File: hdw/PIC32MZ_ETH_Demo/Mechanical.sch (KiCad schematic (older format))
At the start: 24 parts

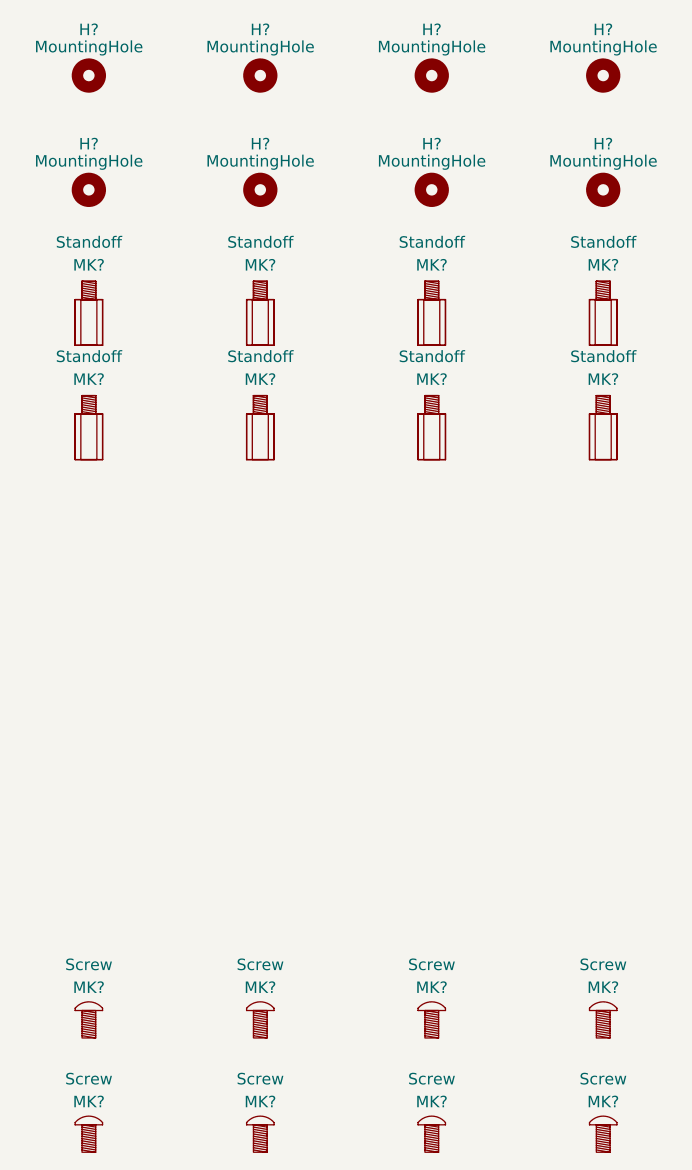
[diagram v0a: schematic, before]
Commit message: More schematic tweaks, followed PHY design guide
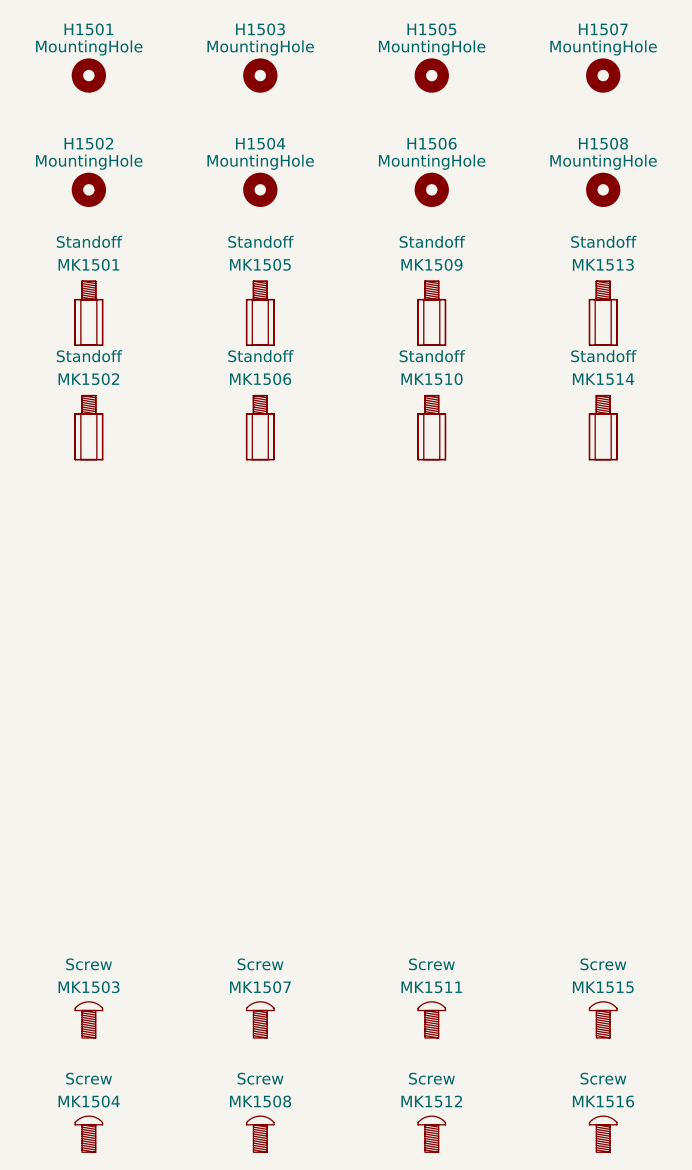
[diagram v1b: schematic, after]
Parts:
- gave numbers to parts that had none: 24
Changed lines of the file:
@@
 EESchema Schematic File Version 4
+LIBS:PIC32MZ_ETH_Demo-cache
 EELAYER 30 0
 EELAYER END
@@
 $EndDescr
 $Comp
-L Mechanical:MountingHole H?
+L Mechanical:MountingHole H1501
 U 1 1 5CC525BF
 P 4070 1580
-F 0 "H?" H 4070 1780 50  0000 C CNN
+F 0 "H1501" H 4070 1780 50  0000 C CNN
 F 1 "MountingHole" H 4070 1705 50  0000 C CNN
 F 2 "MountingHole:MountingHole_3mm" H 4070 1580 50  0001 C CNN
@@
 $EndComp
 $Comp
-L Mechanical:MountingHole H?
+L Mechanical:MountingHole H1503
 U 1 1 5CC5295F
 P 4820 1580
-F 0 "H?" H 4820 1780 50  0000 C CNN
+F 0 "H1503" H 4820 1780 50  0000 C CNN
 F 1 "MountingHole" H 4820 1705 50  0000 C CNN
 F 2 "MountingHole:MountingHole_3mm" H 4820 1580 50  0001 C CNN
@@
 $EndComp
 $Comp
-L Mechanical:MountingHole H?
+L Mechanical:MountingHole H1505
 U 1 1 5CC52BE4
 P 5570 1580
-F 0 "H?" H 5570 1780 50  0000 C CNN
+F 0 "H1505" H 5570 1780 50  0000 C CNN
 F 1 "MountingHole" H 5570 1705 50  0000 C CNN
 F 2 "MountingHole:MountingHole_3mm" H 5570 1580 50  0001 C CNN
@@
 $EndComp
 $Comp
-L Mechanical:MountingHole H?
+L Mechanical:MountingHole H1507
 U 1 1 5CC530EC
 P 6320 1580
-F 0 "H?" H 6320 1780 50  0000 C CNN
+F 0 "H1507" H 6320 1780 50  0000 C CNN
 F 1 "MountingHole" H 6320 1705 50  0000 C CNN
 F 2 "MountingHole:MountingHole_3mm" H 6320 1580 50  0001 C CNN
@@
 $EndComp
 $Comp
-L Mechanical:MountingHole H?
+L Mechanical:MountingHole H1502
 U 1 1 5CC53950
 P 4070 2080
-F 0 "H?" H 4070 2280 50  0000 C CNN
+F 0 "H1502" H 4070 2280 50  0000 C CNN
 F 1 "MountingHole" H 4070 2205 50  0000 C CNN
 F 2 "MountingHole:MountingHole_3mm" H 4070 2080 50  0001 C CNN
@@
 $EndComp
 $Comp
-L Mechanical:MountingHole H?
+L Mechanical:MountingHole H1504
 U 1 1 5CC5395A
 P 4820 2080
-F 0 "H?" H 4820 2280 50  0000 C CNN
+F 0 "H1504" H 4820 2280 50  0000 C CNN
 F 1 "MountingHole" H 4820 2205 50  0000 C CNN
 F 2 "MountingHole:MountingHole_3mm" H 4820 2080 50  0001 C CNN
@@
 $EndComp
 $Comp
-L Mechanical:MountingHole H?
+L Mechanical:MountingHole H1506
 U 1 1 5CC53964
 P 5570 2080
-F 0 "H?" H 5570 2280 50  0000 C CNN
+F 0 "H1506" H 5570 2280 50  0000 C CNN
 F 1 "MountingHole" H 5570 2205 50  0000 C CNN
 F 2 "MountingHole:MountingHole_3mm" H 5570 2080 50  0001 C CNN
@@
 $EndComp
 $Comp
-L Mechanical:MountingHole H?
+L Mechanical:MountingHole H1508
 U 1 1 5CC5396E
 P 6320 2080
-F 0 "H?" H 6320 2280 50  0000 C CNN
+F 0 "H1508" H 6320 2280 50  0000 C CNN
 F 1 "MountingHole" H 6320 2205 50  0000 C CNN
 F 2 "MountingHole:MountingHole_3mm" H 6320 2080 50  0001 C CNN
@@
 $EndComp
 $Comp
-L Custom_Library:Standoff MK?
+L Custom_Library:Standoff MK1501
 U 1 1 5CC56F37
 P 4070 2560
-F 0 "MK?" H 4070 2710 50  0000 C CNN
+F 0 "MK1501" H 4070 2710 50  0000 C CNN
 F 1 "Standoff" H 4070 2810 50  0000 C CNN
 F 2 "" H 4070 2910 50  0001 C CNN
@@
 $EndComp
 $Comp
-L Custom_Library:Standoff MK?
+L Custom_Library:Standoff MK1505
 U 1 1 5CC579C0
 P 4820 2560
-F 0 "MK?" H 4820 2710 50  0000 C CNN
+F 0 "MK1505" H 4820 2710 50  0000 C CNN
 F 1 "Standoff" H 4820 2810 50  0000 C CNN
 F 2 "" H 4820 2910 50  0001 C CNN
@@
 $EndComp
 $Comp
-L Custom_Library:Standoff MK?
+L Custom_Library:Standoff MK1509
 U 1 1 5CC58B78
 P 5570 2560
-F 0 "MK?" H 5570 2710 50  0000 C CNN
+F 0 "MK1509" H 5570 2710 50  0000 C CNN
 F 1 "Standoff" H 5570 2810 50  0000 C CNN
 F 2 "" H 5570 2910 50  0001 C CNN
@@
 $EndComp
 $Comp
-L Custom_Library:Standoff MK?
+L Custom_Library:Standoff MK1513
 U 1 1 5CC59CF0
 P 6320 2560
-F 0 "MK?" H 6320 2710 50  0000 C CNN
+F 0 "MK1513" H 6320 2710 50  0000 C CNN
 F 1 "Standoff" H 6320 2810 50  0000 C CNN
 F 2 "" H 6320 2910 50  0001 C CNN
@@
 $EndComp
 $Comp
-L Custom_Library:Standoff MK?
+L Custom_Library:Standoff MK1502
 U 1 1 5CC5B024
 P 4070 3060
-F 0 "MK?" H 4070 3210 50  0000 C CNN
+F 0 "MK1502" H 4070 3210 50  0000 C CNN
 F 1 "Standoff" H 4070 3310 50  0000 C CNN
 F 2 "" H 4070 3410 50  0001 C CNN
@@
 $EndComp
 $Comp
-L Custom_Library:Standoff MK?
+L Custom_Library:Standoff MK1506
 U 1 1 5CC5B02E
 P 4820 3060
-F 0 "MK?" H 4820 3210 50  0000 C CNN
+F 0 "MK1506" H 4820 3210 50  0000 C CNN
 F 1 "Standoff" H 4820 3310 50  0000 C CNN
 F 2 "" H 4820 3410 50  0001 C CNN
@@
 $EndComp
 $Comp
-L Custom_Library:Standoff MK?
+L Custom_Library:Standoff MK1510
 U 1 1 5CC5B038
 P 5570 3060
-F 0 "MK?" H 5570 3210 50  0000 C CNN
+F 0 "MK1510" H 5570 3210 50  0000 C CNN
 F 1 "Standoff" H 5570 3310 50  0000 C CNN
 F 2 "" H 5570 3410 50  0001 C CNN
@@
 $EndComp
 $Comp
-L Custom_Library:Standoff MK?
+L Custom_Library:Standoff MK1514
 U 1 1 5CC5B042
 P 6320 3060
-F 0 "MK?" H 6320 3210 50  0000 C CNN
+F 0 "MK1514" H 6320 3210 50  0000 C CNN
 F 1 "Standoff" H 6320 3310 50  0000 C CNN
 F 2 "" H 6320 3410 50  0001 C CNN
@@
 $EndComp
 $Comp
-L Custom_Library:Screw MK?
+L Custom_Library:Screw MK1503
 U 1 1 5CC6CBF3
 P 4070 5670
-F 0 "MK?" H 4070 5770 50  0000 C CNN
+F 0 "MK1503" H 4070 5770 50  0000 C CNN
 F 1 "Screw" H 4070 5870 50  0000 C CNN
 F 2 "" H 4070 5920 50  0001 C CNN
@@
 $EndComp
 $Comp
-L Custom_Library:Screw MK?
+L Custom_Library:Screw MK1507
 U 1 1 5CC6D1A5
 P 4820 5670
-F 0 "MK?" H 4820 5770 50  0000 C CNN
+F 0 "MK1507" H 4820 5770 50  0000 C CNN
 F 1 "Screw" H 4820 5870 50  0000 C CNN
 F 2 "" H 4820 5920 50  0001 C CNN
@@
 $EndComp
 $Comp
-L Custom_Library:Screw MK?
+L Custom_Library:Screw MK1511
 U 1 1 5CC6E4BD
 P 5570 5670
-F 0 "MK?" H 5570 5770 50  0000 C CNN
+F 0 "MK1511" H 5570 5770 50  0000 C CNN
 F 1 "Screw" H 5570 5870 50  0000 C CNN
 F 2 "" H 5570 5920 50  0001 C CNN
@@
 $EndComp
 $Comp
-L Custom_Library:Screw MK?
+L Custom_Library:Screw MK1515
 U 1 1 5CC6F609
 P 6320 5670
-F 0 "MK?" H 6320 5770 50  0000 C CNN
+F 0 "MK1515" H 6320 5770 50  0000 C CNN
 F 1 "Screw" H 6320 5870 50  0000 C CNN
 F 2 "" H 6320 5920 50  0001 C CNN
@@
 $EndComp
 $Comp
-L Custom_Library:Screw MK?
+L Custom_Library:Screw MK1504
 U 1 1 5CC70A99
 P 4070 6170
-F 0 "MK?" H 4070 6270 50  0000 C CNN
+F 0 "MK1504" H 4070 6270 50  0000 C CNN
 F 1 "Screw" H 4070 6370 50  0000 C CNN
 F 2 "" H 4070 6420 50  0001 C CNN
@@
 $EndComp
 $Comp
-L Custom_Library:Screw MK?
+L Custom_Library:Screw MK1508
 U 1 1 5CC70AA3
 P 4820 6170
-F 0 "MK?" H 4820 6270 50  0000 C CNN
+F 0 "MK1508" H 4820 6270 50  0000 C CNN
 F 1 "Screw" H 4820 6370 50  0000 C CNN
 F 2 "" H 4820 6420 50  0001 C CNN
@@
 $EndComp
 $Comp
-L Custom_Library:Screw MK?
+L Custom_Library:Screw MK1512
 U 1 1 5CC70AAD
 P 5570 6170
-F 0 "MK?" H 5570 6270 50  0000 C CNN
+F 0 "MK1512" H 5570 6270 50  0000 C CNN
 F 1 "Screw" H 5570 6370 50  0000 C CNN
 F 2 "" H 5570 6420 50  0001 C CNN
@@
 $EndComp
 $Comp
-L Custom_Library:Screw MK?
+L Custom_Library:Screw MK1516
 U 1 1 5CC70AB7
 P 6320 6170
-F 0 "MK?" H 6320 6270 50  0000 C CNN
+F 0 "MK1516" H 6320 6270 50  0000 C CNN
 F 1 "Screw" H 6320 6370 50  0000 C CNN
 F 2 "" H 6320 6420 50  0001 C CNN

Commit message: Finished board layout
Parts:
- removed H1506, H1507, H1508: MountingHole, MountingHole:MountingHole_3mm, symbol Mechanical:MountingHole
- removed MK1510, MK1513, MK1514: Standoff, symbol Custom_Library:Standoff
- removed MK1512, MK1515, MK1516: Screw, symbol Custom_Library:Screw
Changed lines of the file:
@@
-$EndComp
-$Comp
-L Mechanical:MountingHole H1507
-U 1 1 5CC530EC
-P 6320 1580
-F 0 "H1507" H 6320 1780 50  0000 C CNN
-F 1 "MountingHole" H 6320 1705 50  0000 C CNN
-F 2 "MountingHole:MountingHole_3mm" H 6320 1580 50  0001 C CNN
-F 3 "~" H 6320 1580 50  0001 C CNN
-	1    6320 1580
-	1    0    0    -1
 $EndComp
 $Comp
@@
 F 3 "~" H 4820 2080 50  0001 C CNN
 	1    4820 2080
-	1    0    0    -1
-$EndComp
-$Comp
-L Mechanical:MountingHole H1506
-U 1 1 5CC53964
-P 5570 2080
-F 0 "H1506" H 5570 2280 50  0000 C CNN
-F 1 "MountingHole" H 5570 2205 50  0000 C CNN
-F 2 "MountingHole:MountingHole_3mm" H 5570 2080 50  0001 C CNN
-F 3 "~" H 5570 2080 50  0001 C CNN
-	1    5570 2080
-	1    0    0    -1
-$EndComp
-$Comp
-L Mechanical:MountingHole H1508
-U 1 1 5CC5396E
-P 6320 2080
-F 0 "H1508" H 6320 2280 50  0000 C CNN
-F 1 "MountingHole" H 6320 2205 50  0000 C CNN
-F 2 "MountingHole:MountingHole_3mm" H 6320 2080 50  0001 C CNN
-F 3 "~" H 6320 2080 50  0001 C CNN
-	1    6320 2080
 	1    0    0    -1
 $EndComp
@@
 $EndComp
 $Comp
-L Custom_Library:Standoff MK1513
-U 1 1 5CC59CF0
-P 6320 2560
-F 0 "MK1513" H 6320 2710 50  0000 C CNN
-F 1 "Standoff" H 6320 2810 50  0000 C CNN
-F 2 "" H 6320 2910 50  0001 C CNN
-F 3 "" H 6320 2910 50  0001 C CNN
-F 4 "1772-2080-ND" H 6320 2560 50  0001 C CNN "Digi-Key PN"
-	1    6320 2560
-	1    0    0    -1
-$EndComp
-$Comp
 L Custom_Library:Standoff MK1502
 U 1 1 5CC5B024
@@
 F 4 "1772-2080-ND" H 4820 3060 50  0001 C CNN "Digi-Key PN"
 	1    4820 3060
-	1    0    0    -1
-$EndComp
-$Comp
-L Custom_Library:Standoff MK1510
-U 1 1 5CC5B038
-P 5570 3060
-F 0 "MK1510" H 5570 3210 50  0000 C CNN
-F 1 "Standoff" H 5570 3310 50  0000 C CNN
-F 2 "" H 5570 3410 50  0001 C CNN
-F 3 "" H 5570 3410 50  0001 C CNN
-F 4 "1772-2080-ND" H 5570 3060 50  0001 C CNN "Digi-Key PN"
-	1    5570 3060
-	1    0    0    -1
-$EndComp
-$Comp
-L Custom_Library:Standoff MK1514
-U 1 1 5CC5B042
-P 6320 3060
-F 0 "MK1514" H 6320 3210 50  0000 C CNN
-F 1 "Standoff" H 6320 3310 50  0000 C CNN
-F 2 "" H 6320 3410 50  0001 C CNN
-F 3 "" H 6320 3410 50  0001 C CNN
-F 4 "1772-2080-ND" H 6320 3060 50  0001 C CNN "Digi-Key PN"
-	1    6320 3060
 	1    0    0    -1
 $EndComp
@@
 $EndComp
 $Comp
-L Custom_Library:Screw MK1515
-U 1 1 5CC6F609
-P 6320 5670
-F 0 "MK1515" H 6320 5770 50  0000 C CNN
-F 1 "Screw" H 6320 5870 50  0000 C CNN
-F 2 "" H 6320 5920 50  0001 C CNN
-F 3 "" H 6320 5920 50  0001 C CNN
-F 4 "36-9900-ND" H 6320 5670 50  0001 C CNN "Digi-Key PN"
-	1    6320 5670
-	1    0    0    -1
-$EndComp
-$Comp
 L Custom_Library:Screw MK1504
 U 1 1 5CC70A99
@@
 	1    0    0    -1
 $EndComp
-$Comp
-L Custom_Library:Screw MK1512
-U 1 1 5CC70AAD
-P 5570 6170
-F 0 "MK1512" H 5570 6270 50  0000 C CNN
-F 1 "Screw" H 5570 6370 50  0000 C CNN
-F 2 "" H 5570 6420 50  0001 C CNN
-F 3 "" H 5570 6420 50  0001 C CNN
-F 4 "36-9900-ND" H 5570 6170 50  0001 C CNN "Digi-Key PN"
-	1    5570 6170
-	1    0    0    -1
-$EndComp
-$Comp
-L Custom_Library:Screw MK1516
-U 1 1 5CC70AB7
-P 6320 6170
-F 0 "MK1516" H 6320 6270 50  0000 C CNN
-F 1 "Screw" H 6320 6370 50  0000 C CNN
-F 2 "" H 6320 6420 50  0001 C CNN
-F 3 "" H 6320 6420 50  0001 C CNN
-F 4 "36-9900-ND" H 6320 6170 50  0001 C CNN "Digi-Key PN"
-	1    6320 6170
-	1    0    0    -1
-$EndComp
